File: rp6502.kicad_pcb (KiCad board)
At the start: 2 copper layers, 150 x 100 mm, 55 parts, among them J1 AUDIO, J2 VGA, J3 REBOOT, J4 GPIO, J5 PIX, U1 W65C02S, U2 Pico RIA, U3 AS6C1008, U4 Pico VGA, U5 W65C22S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

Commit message: pcb beauty
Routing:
- net GND: track 845.1 -> 865.0 mm
- net Net-(JP1-A): track 27.7 -> 38.3 mm, vias 0 -> 1
- net /RWB: track 224.3 -> 233.4 mm
- net /A4: track 139.3 -> 133.4 mm
- net /A6: track 147.8 -> 142.0 mm
- net /A3: track 175.0 -> 169.5 mm
- net /A1: track 199.9 -> 194.7 mm
- net /WE#: track 104.1 -> 99.2 mm
- net /RESB: track 112.6 -> 116.7 mm
- net /BLU2: track 65.2 -> 69.2 mm
- net /IRQB: track 80.8 -> 76.9 mm
- net Net-(C11-Pad1): track 36.7 -> 40.4 mm
- net /A7: track 131.4 -> 127.7 mm
- net /BLU0: track 58.1 -> 61.8 mm
- net /BLU3: track 67.3 -> 70.9 mm
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
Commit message: pcb complete
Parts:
- R18: value 8.06K -> 8.06k
- R21, R24: value 1.8K -> 1.8k
- moved REF** 90.9 mm to (209.7, 61.5)
- moved REF** 90.5 mm to (209.7, 151.5)
- moved REF** 1.02 mm to (69.7, 151.5)
- moved REF** 0.73 mm to (69.7, 61.5)
- moved JP1 0.63 mm to (117.5, 66.0)
- moved JP2 0.63 mm to (117.5, 69.8)
- moved SW1 0.32 mm to (105.7, 59.7)
- renumbered J4 to J1, J5 to J2, J2 to J3, J1 to J4, J3 to SW1
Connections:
- U6 pad 12: /A7 -> /A5
- U6 pad 9: /A5 -> /A7
- U7 pad 10: /IRQB -> Net-(U6-Pad2)
- U7 pad 11: /RWB -> Net-(U6-Pad6)
- U7 pad 13: Net-(U6-Pad2) -> /IRQB
- U7 pad 8: Net-(U6-Pad6) -> /RWB
- U8 pad 1: /A8 -> /A9
- U8 pad 11: /A14 -> /A15
- U8 pad 12: /A15 -> /A8
- U8 pad 2: /A9 -> /A10
- U8 pad 3: /A10 -> /A11
- U8 pad 4: /A11 -> /A12
- U8 pad 5: /A12 -> /A13
- U8 pad 6: /A13 -> /A14
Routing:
- net /WE#: track 99.2 -> 84.4 mm
- net Net-(U6-Pad2): track 6.37 -> 17.6 mm
- net /A5: track 126.0 -> 118.0 mm
- net /RIRQB: track 39.4 -> 45.9 mm
- net /IRQB: track 76.9 -> 70.7 mm
- net /A9: track 61.3 -> 55.3 mm
- net /A14: track 84.7 -> 90.7 mm
- net /A8: track 59.0 -> 64.6 mm
- net Net-(U6-Pad8): track 33.3 -> 37.9 mm
- net /RWB: track 233.4 -> 237.0 mm
- net /A10: track 59.7 -> 56.2 mm
- net /A15: track 66.3 -> 69.5 mm
- net /A12: track 93.6 -> 90.5 mm
- net /A11: track 67.1 -> 64.3 mm
- net /A7: track 127.7 -> 130.4 mm
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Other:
- board size 150 x 100 mm -> 149.9 x 99.8 mm
- board text added: "Mark Rowe Sean Franklin Larryvc Vitali Filinkou Romain Fontaine Shawn Hyam Andy Herron ulften"
- board text added: "USB to host or power supply"
- board text added: "USB to hub or device"

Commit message: founders edition
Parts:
- moved J1 0.64 mm to (77.5, 115.6)
- moved J2 0.64 mm to (92.7, 115.6)
- moved REF** 0.18 mm to (69.7, 151.7)
- moved REF** 0.18 mm to (209.7, 151.7)
- moved REF** 0.18 mm to (209.7, 61.7)
- moved REF** 0.18 mm to (69.7, 61.7)
- moved J4 0.08 mm to (169.5, 61.2)
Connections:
- U8 pad 10: (no net) -> unconnected-(U8A-NC-Pad10)
- U8 pad 13: (no net) -> unconnected-(U8A-NC-Pad13)
- U8 pad 9: (no net) -> unconnected-(U8A-NC-Pad9)
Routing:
- net /PA5: track 41.6 -> 40.2 mm
- net /PA4: track 44.1 -> 42.8 mm
- net /PA3: track 46.7 -> 45.4 mm
- net /PA1: track 51.9 -> 50.6 mm
- net /PA2: track 49.3 -> 48.0 mm
- net /PA0: track 54.4 -> 53.2 mm
- net GND: track 865.6 -> 864.6 mm
- net +3V3B: track 159.1 -> 158.4 mm
- net /PA6: track 39.0 -> 38.4 mm
- net /PA7: track 38.0 -> 37.4 mm
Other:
- board size 149.9 x 99.8 mm -> 150 x 100 mm
- board text added: "David Turnbull Mark Rowe Sean Franklin Larryvc Vitali Filinkou Romain Fontaine Shawn Hyam Andy Herron ulften"
- board text added: "Founders Edition"
- board text removed: "Mark Rowe Sean Franklin Larryvc Vitali Filinkou Romain Fontaine Shawn Hyam Andy Herron ulften"
- board text removed: "Patreon Edition Rev. 1"

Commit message: first assembly
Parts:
- J3: footprint Connector_Dsub:DSUB-15-HD_Female_Horizontal_P2.29x1.98mm_EdgePinOffset8.35mm_Housed_MountingHolesOffset10.89mm -> rp6502:DSUB-15-HD_Female_Horizontal_P2.29x2.54mm_EdgePinOffset8.35mm_Housed_MountingHolesOffset10.89mm
- moved J3 1.61 mm to (135.4, 70.6)
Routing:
- net Net-(JP1-A): track 37.6 -> 24.9 mm, vias 1 -> 0
- net GND: track 864.6 -> 862.5 mm
- net /REDV: track 37.8 -> 36.0 mm
- net /GRNV: track 29.2 -> 27.6 mm
- net /BLUV: track 34.4 -> 33.2 mm
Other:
- board text added: "RP6502 Rev. A"
- board text removed: "David Turnbull Mark Rowe Sean Franklin Larryvc Vitali Filinkou Romain Fontaine Shawn Hyam Andy Herron ulften"
- board text removed: "Founders Edition"

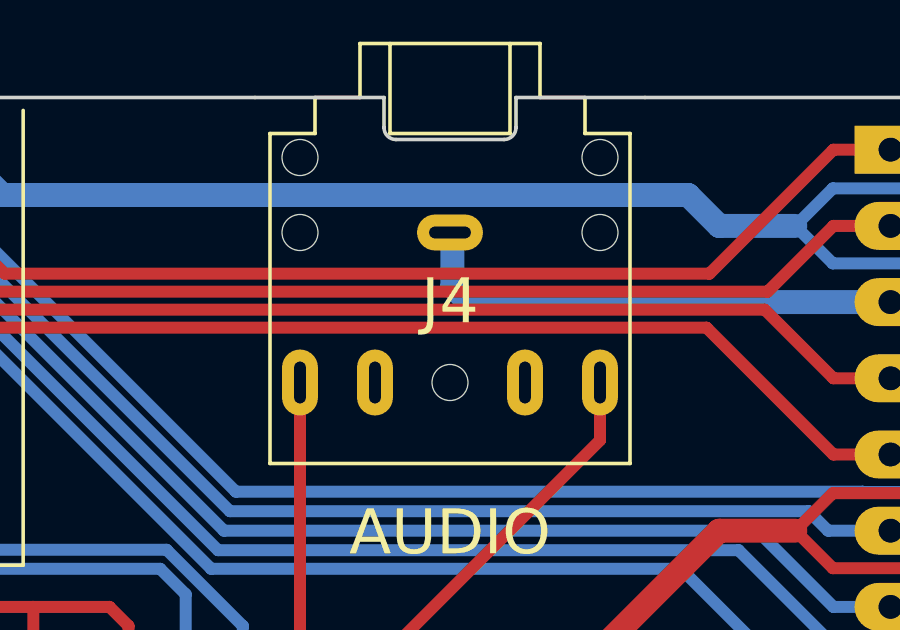
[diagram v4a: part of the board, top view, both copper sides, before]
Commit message: PTH slot increase for PCBWay
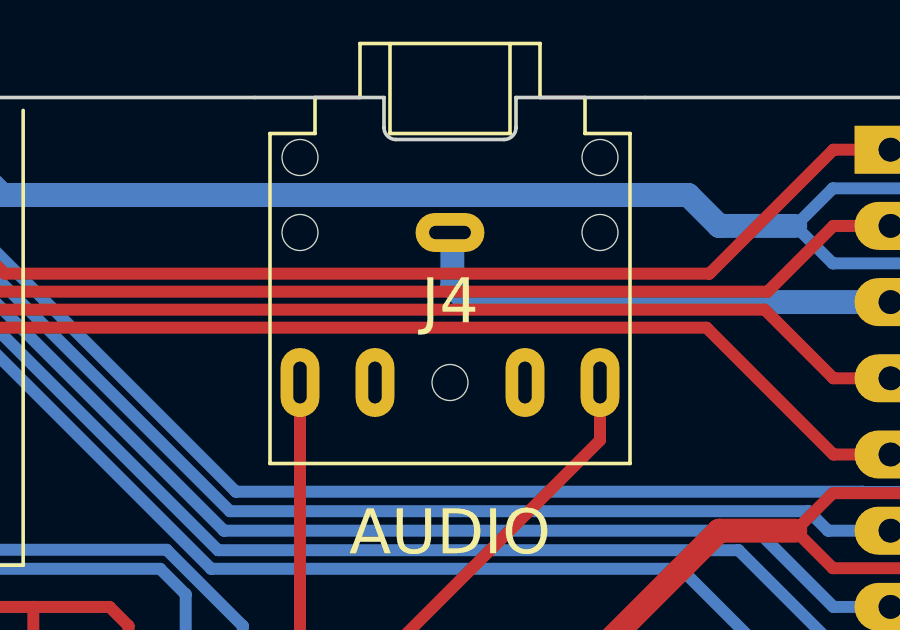
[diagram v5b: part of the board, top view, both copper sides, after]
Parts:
- J4: footprint Connector_Audio:Jack_3.5mm_CUI_SJ1-3525N_Horizontal -> rp6502:Jack_3.5mm_CUI_SJ1-3525N_Horizontal
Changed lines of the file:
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@@
     )
   )
-  (footprint "Connector_Audio:Jack_3.5mm_CUI_SJ1-3525N_Horizontal" (layer "F.Cu")
+  (footprint "rp6502:Jack_3.5mm_CUI_SJ1-3525N_Horizontal" (layer "F.Cu")
     (at 169.465 61.18 180)
     (descr "TRS 3.5mm, horizontal, through-hole, https://www.cuidevices.com/product/resource/pdf/sj1-352xn.pdf")
@@
     (pad "" np_thru_hole circle (at 5 0 180) (size 1.2 1.2) (drill 1.2) (layers "*.Cu"))
     (pad "" np_thru_hole circle (at 5 2.5 180) (size 1.2 1.2) (drill 1.2) (layers "*.Cu"))
-    (pad "R" thru_hole oval (at -5 -5 180) (size 1.2 2.2) (drill oval 0.4 1.4) (layers "*.Cu" "*.Mask")
+    (pad "R" thru_hole oval (at -5 -5 180) (size 1.3 2.3) (drill oval 0.45 1.4) (layers "*.Cu" "*.Mask")
       (net 6 "/AUDR") (pintype "passive"))
-    (pad "RN" thru_hole oval (at -2.5 -5 180) (size 1.2 2.2) (drill oval 0.4 1.4) (layers "*.Cu" "*.Mask")
+    (pad "RN" thru_hole oval (at -2.5 -5 180) (size 1.3 2.3) (drill oval 0.45 1.4) (layers "*.Cu" "*.Mask")
       (net 121 "unconnected-(J4-PadRN)") (pintype "passive+no_connect"))
-    (pad "S" thru_hole oval (at 0 0 180) (size 2.2 1.2) (drill oval 1.4 0.4) (layers "*.Cu" "*.Mask")
+    (pad "S" thru_hole oval (at 0 0 180) (size 2.3 1.3) (drill oval 1.4 0.45) (layers "*.Cu" "*.Mask")
       (net 21 "GND") (pintype "passive"))
-    (pad "T" thru_hole oval (at 5 -5) (size 1.2 2.2) (drill oval 0.4 1.4) (layers "*.Cu" "*.Mask")
+    (pad "T" thru_hole oval (at 5 -5) (size 1.3 2.3) (drill oval 0.45 1.4) (layers "*.Cu" "*.Mask")
       (net 4 "/AUDL") (pintype "passive"))
-    (pad "TN" thru_hole oval (at 2.5 -5) (size 1.2 2.2) (drill oval 0.4 1.4) (layers "*.Cu" "*.Mask")
+    (pad "TN" thru_hole oval (at 2.5 -5) (size 1.3 2.3) (drill oval 0.45 1.4) (layers "*.Cu" "*.Mask")
       (net 122 "unconnected-(J4-PadTN)") (pintype "passive+no_connect"))
     (model "${KICAD6_3DMODEL_DIR}/Connector_Audio.3dshapes/Jack_3.5mm_CUI_SJ1-3525N_Horizontal.wrl"

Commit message: revb
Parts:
- added REF**: OSHW-Logo_11.4x12mm_SilkScreen, Symbol:OSHW-Logo_11.4x12mm_SilkScreen, F.Cu at (94.0, 143.8)
- U2: value Pico RIA -> RP6502-RIA; footprint rp6502:DIP-40_W17.78mm_LongPads_PicoDebug -> rp6502:DIP-40_W17.78mm_LongPads
- U4: value Pico VGA -> RP6502-VGA
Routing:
- net /SWCLK: track 153.5 -> 0.00 mm
- net /SWDIO: track 139.9 -> 0.00 mm
- net GND: track 862.5 -> 839.9 mm
- net VBUS: track 212.8 -> 213.7 mm
- net /UTX: track 123.1 -> 122.2 mm
- net /URX: track 117.2 -> 116.3 mm
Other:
- board text added: "Picocomputer 6502"
- board text added: "Rev. B"
- board text removed: "RP6502 Rev. A"
